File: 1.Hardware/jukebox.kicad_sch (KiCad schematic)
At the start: 32 parts, among them J1 USB_B_Micro, Q1 SS8050, Q2 SS8050, SW1 SW_Push, SW2 SW_Push, U1 CP2102N-Axx-xQFN28, U4 AMS1117-3.3

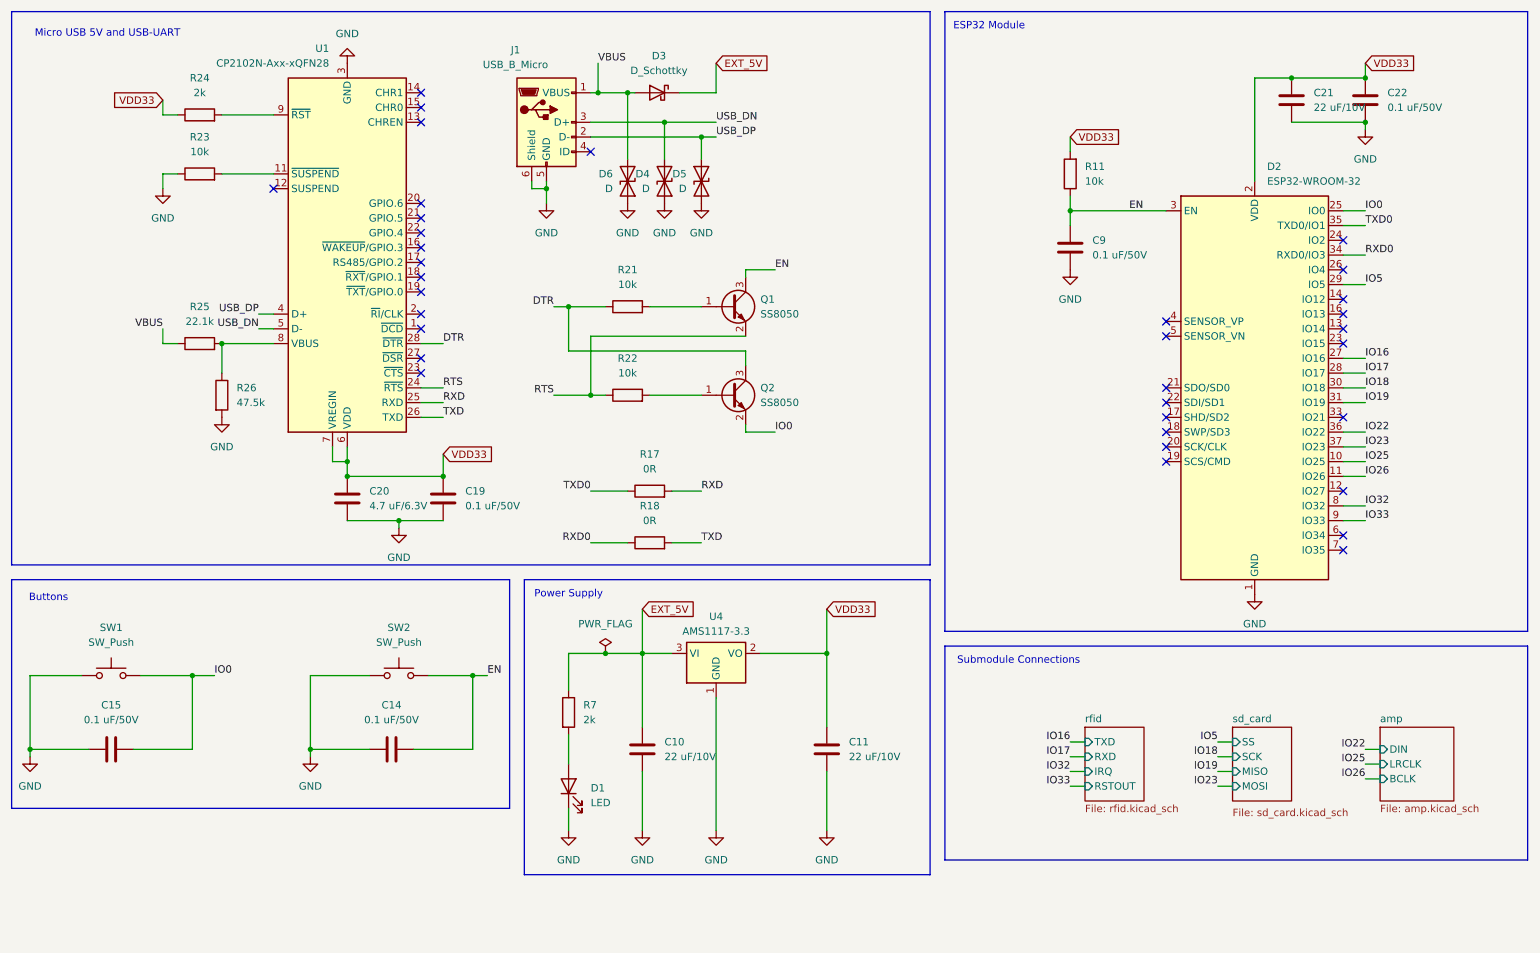
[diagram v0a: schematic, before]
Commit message: changed to usb c
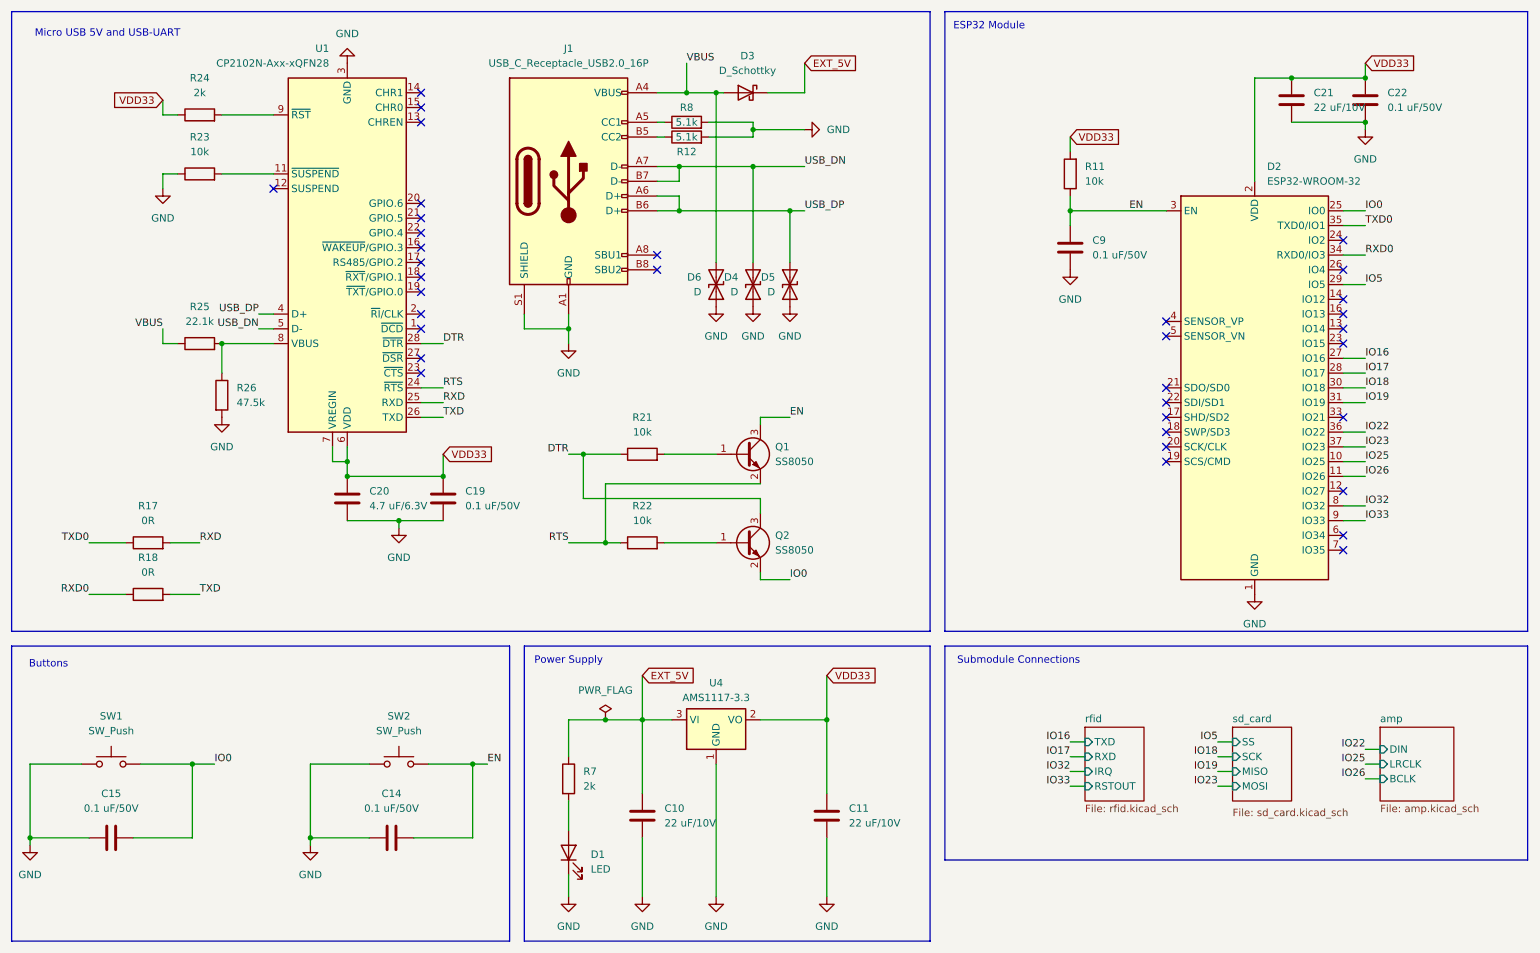
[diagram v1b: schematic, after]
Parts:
- removed J1: USB_B_Micro, Connector_USB:USB_Micro-AB_Molex_47590-0001, symbol Connector:USB_B_Micro
- added J1: USB_C_Receptacle_USB2.0_16P, Connector_USB:USB_C_Receptacle_GCT_USB4105-xx-A_16P_TopMnt_Horizontal, symbol Connector:USB_C_Receptacle_USB2.0_16P
- added R12, R8: 5.1k, symbol Device:R
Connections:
- net GND: now also J1.A1 (GND), J1.A12 (GND), J1.B1 (GND), J1.B12 (GND), J1.S1 (SHIELD), R12.2, R8.2
- net USB_DN: now also J1.A7 (D-), J1.B7 (D-)
- net USB_DP: now also J1.A6 (D+), J1.B6 (D+)
- net VBUS: now also J1.A4 (VBUS), J1.A9 (VBUS), J1.B4 (VBUS), J1.B9 (VBUS)
- new net: J1.B5 (CC2), R12.1
- new net: J1.A5 (CC1), R8.1
- no-connect marks 34 -> 35
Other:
- moved on the sheet: C10, C11, C14, C15, D1, D3, D4, D5, D6, Q1, Q2, R17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

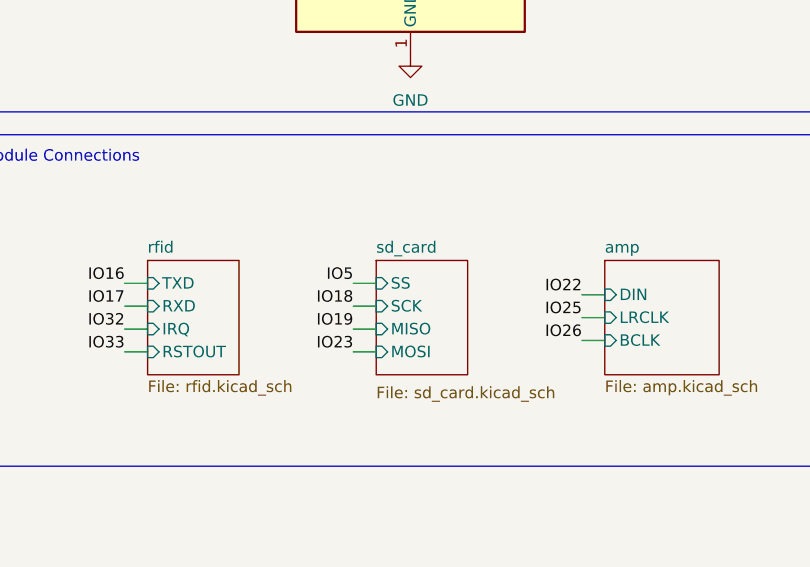
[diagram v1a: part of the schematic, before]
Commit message: updated schematic to match demo
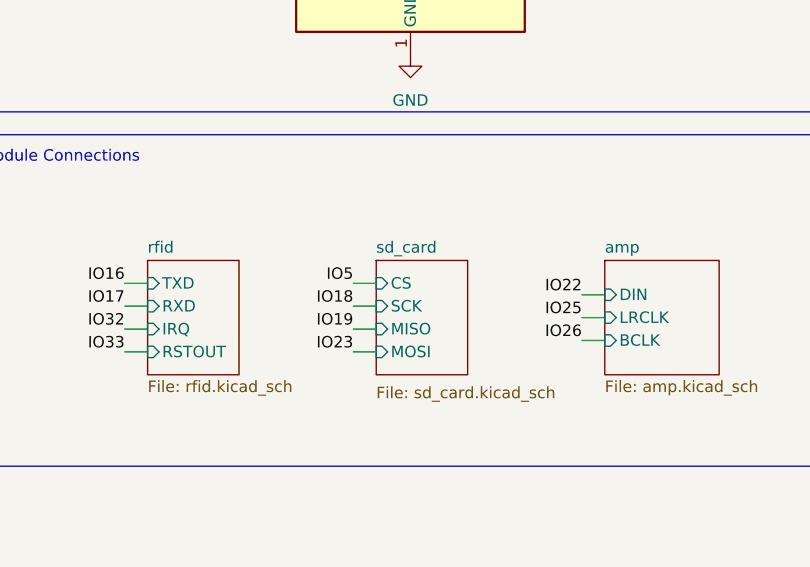
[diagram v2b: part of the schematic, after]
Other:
- sheet sd_card ports: added CS; removed SS
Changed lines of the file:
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@@
 			)
 		)
-		(pin "SS" input
+		(pin "CS" input
 			(at 228.6 142.24 180)
 			(effects

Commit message: ready for routing/placement
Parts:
- added J2: S4B-XH-A, S4B-XH-A:JST_S4B-XH-A, symbol S4B-XH-A:S4B-XH-A
- added J3: B3B-XH-A, B3B_XH_A:JST_B3B-XH-A, symbol B3B-XH-A:B3B-XH-A
- added J5: Conn_01x10_Socket, Connector_PinHeader_2.54mm:PinHeader_1x10_P2.54mm_Vertical, symbol Connector:Conn_01x10_Socket
- added RV2: 10k, 3306K:TRIM_3306K-1-202, symbol Device:R_Potentiometer
- C10, C11, C21: footprint Capacitor_SMD:C_0603_1608Metric -> Capacitor_SMD:C_0603_1608Metric_Pad1.08x0.95mm_HandSolder
- C14, C15, C19, C20, C22, C9: footprint Capacitor_SMD:C_0402_1005Metric -> Capacitor_SMD:C_0603_1608Metric_Pad1.08x0.95mm_HandSolder
- D1: footprint LED_SMD:LED_0603_1608Metric -> LED_SMD:LED_0603_1608Metric_Pad1.05x0.95mm_HandSolder
- R11, R17, R18, R21, R22, R23, R24, R25, R26, R7: footprint Resistor_SMD:R_0402_1005Metric -> Resistor_SMD:R_0603_1608Metric_Pad0.98x0.95mm_HandSolder
- R12, R8: footprint (none) -> Resistor_SMD:R_0603_1608Metric_Pad0.98x0.95mm_HandSolder
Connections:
- net GND: now also J2.1, J3.3, RV2.3
- net IO16: now also J2.3
- net IO17: now also J2.4
- net VDD33: now also J2.2, RV2.1
- net at D2.12 (IO27): now also J5.8 (Pin_8)
- net at D2.13 (IO14): now also J5.5 (Pin_5)
- net at D2.14 (IO12): now also J5.3 (Pin_3)
- net at D2.16 (IO13): now also J5.4 (Pin_4)
- net at D2.23 (IO15): now also J5.6 (Pin_6)
- net at D2.24 (IO2): now also J5.1 (Pin_1)
- net at D2.26 (IO4): now also J5.2 (Pin_2)
- net at D2.33 (IO21): now also J5.7 (Pin_7)
- net at D2.6 (IO34): now also RV2.2
- net at D2.7 (IO35): now also J5.10 (Pin_10)
- net IO32: no longer names the net of D2.8 (IO32)
- net IO32: now also J3.2
- net IO33: no longer names the net of D2.9 (IO33)
- net IO33: now also J5.9 (Pin_9)
- no-connect marks 35 -> 26
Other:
- removed sheet rfid
- moved on the sheet: C21, C22, C9, D2, R11
